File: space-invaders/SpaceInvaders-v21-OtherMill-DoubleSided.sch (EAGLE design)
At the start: 26 parts, among them J2-J4 TM4C123GXL, J3-J1 TM4C123GXL, J5 NOKIA_5110, J6 NOKIA_5110, J7 9V, U1 LM7805CT

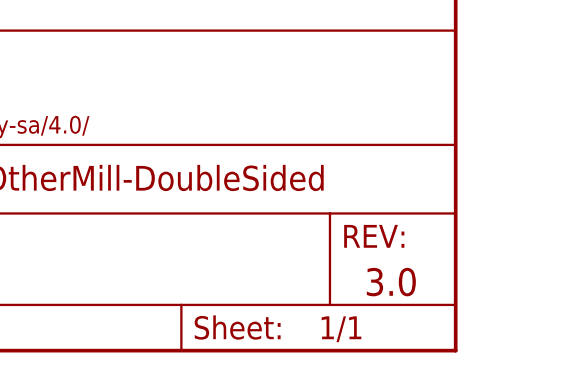
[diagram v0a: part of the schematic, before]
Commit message: Add versions to file names & Edit stuff
Add versions to file names.
Center Nokia5110 & Edit traces thereof.
Add holes for 9V battery's wires to come through.
v2.1: Replace "SpaceInvaders," "by PhiL," and the sprite icon by Top &
Bottom layers.
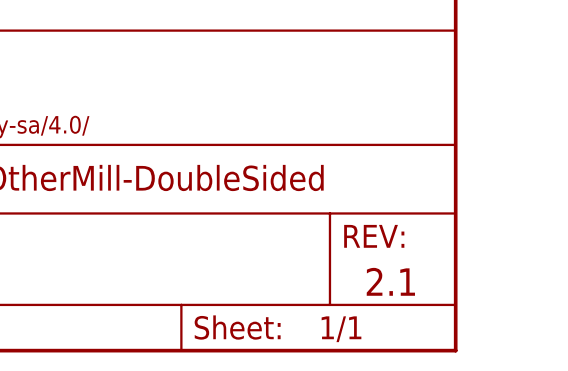
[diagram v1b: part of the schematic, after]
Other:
- note added: "2.1"
- note removed: "3.0"
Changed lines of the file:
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@@
 <plain>
 <text x="172.72" y="12.7" size="3.048" layer="94" font="vector" align="center-left">Phi Luu</text>
-<text x="238.76" y="7.62" size="3.048" layer="94" font="vector" align="center-left">3.0</text>
+<text x="238.76" y="7.62" size="3.048" layer="94" font="vector" align="center-left">2.1</text>
 <text x="134.62" y="147.32" size="1.778" layer="96" font="vector" rot="R90">PB0</text>
 <text x="132.08" y="147.32" size="1.778" layer="96" font="vector" rot="R90">PB1</text>

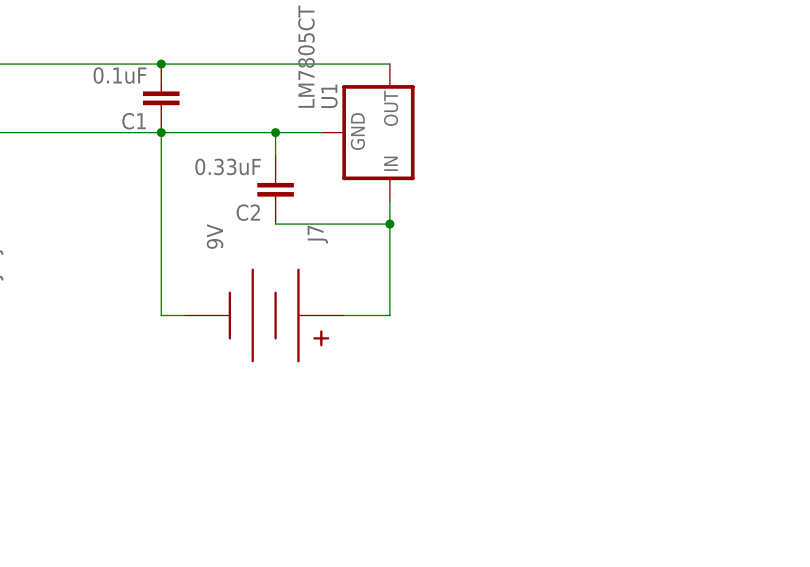
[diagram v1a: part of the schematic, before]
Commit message: Add SPDT power switch
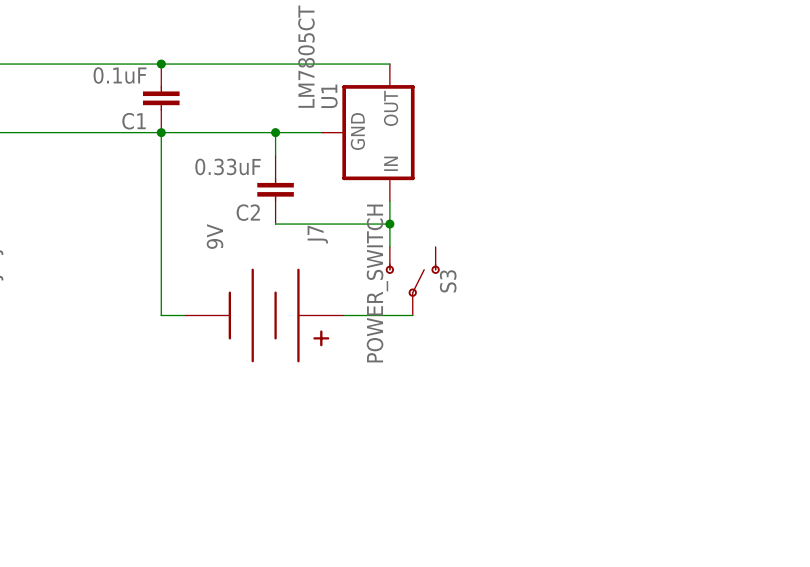
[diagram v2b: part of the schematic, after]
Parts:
- added S3: POWER_SWITCH, SparkFun-Switches:SWITCH-SPDT-PTH-11.6X4.0MM
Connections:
- new net VIN: J7.V+, S3.P
- net 9V: now also S3.S; no longer J7.V+
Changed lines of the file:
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@@
 <?xml version="1.0" encoding="utf-8"?>
 <!DOCTYPE eagle SYSTEM "eagle.dtd">
-<eagle version="8.0.1">
+<eagle version="8.0.2">
 <drawing>
 <settings>
@@
 <part name="S1" library="SparkFun-Switches" deviceset="MOMENTARY-SWITCH-SPST" device="-PTH-6.0MM" value="SPECIAL"/>
 <part name="S2" library="SparkFun-Switches" deviceset="MOMENTARY-SWITCH-SPST" device="-PTH-6.0MM" value="REGULAR"/>
+<part name="S3" library="SparkFun-Switches" deviceset="SWITCH-SPDT" device="-PTH-11.6X4.0MM" value="POWER_SWITCH"/>
 </parts>
 <sheets>
@@
 <instance part="S1" gate="G$1" x="101.6" y="50.8"/>
 <instance part="S2" gate="G$1" x="121.92" y="50.8"/>
+<instance part="S3" gate="1" x="190.5" y="101.6" rot="MR90"/>
 </instances>
 <busses>
@@
 <wire x1="187.96" y1="109.22" x2="187.96" y2="111.76" width="0.1524" layer="91"/>
 <wire x1="175.26" y1="109.22" x2="187.96" y2="109.22" width="0.1524" layer="91"/>
-<wire x1="187.96" y1="99.06" x2="187.96" y2="109.22" width="0.1524" layer="91"/>
+<pinref part="S3" gate="1" pin="S"/>
+<wire x1="187.96" y1="106.68" x2="187.96" y2="109.22" width="0.1524" layer="91"/>
 <junction x="187.96" y="109.22"/>
-<pinref part="J7" gate="G$1" pin="V+"/>
-<wire x1="182.88" y1="99.06" x2="187.96" y2="99.06" width="0.1524" layer="91"/>
 </segment>
 </net>
@@
 </segment>
 </net>
+<net name="VIN" class="1">
+<segment>
+<pinref part="J7" gate="G$1" pin="V+"/>
+<wire x1="182.88" y1="99.06" x2="190.5" y2="99.06" width="0.1524" layer="91"/>
+<pinref part="S3" gate="1" pin="P"/>
+</segment>
+</net>

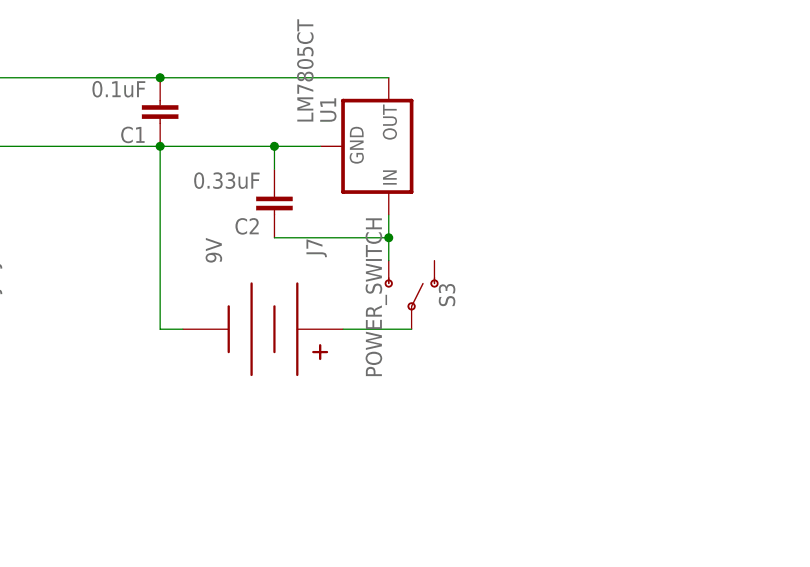
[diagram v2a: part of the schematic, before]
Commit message: Change pin position SPDT slide switch
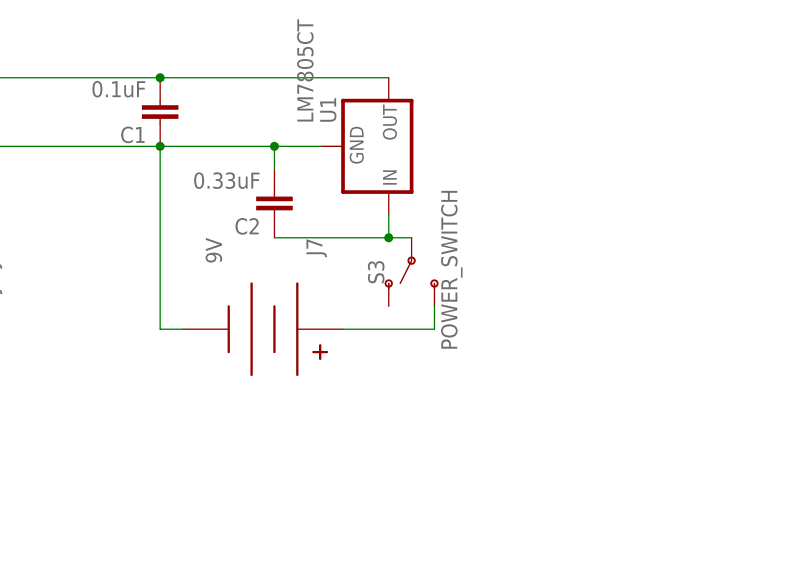
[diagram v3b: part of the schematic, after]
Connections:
- net 9V: now also J7.V+; no longer C2.1, U1.IN
- net VIN: now also C2.1, U1.IN; no longer J7.V+
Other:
- moved on the sheet: S3
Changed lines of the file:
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@@
 <instance part="S1" gate="G$1" x="101.6" y="50.8"/>
 <instance part="S2" gate="G$1" x="121.92" y="50.8"/>
-<instance part="S3" gate="1" x="190.5" y="101.6" rot="MR90"/>
+<instance part="S3" gate="1" x="190.5" y="106.68" rot="MR270"/>
 </instances>
 <busses>
@@
 </segment>
 </net>
-<net name="9V" class="1">
+<net name="VIN" class="1">
 <segment>
 <pinref part="U1" gate="G$1" pin="IN"/>
@@
 <wire x1="187.96" y1="109.22" x2="187.96" y2="111.76" width="0.1524" layer="91"/>
 <wire x1="175.26" y1="109.22" x2="187.96" y2="109.22" width="0.1524" layer="91"/>
-<pinref part="S3" gate="1" pin="S"/>
-<wire x1="187.96" y1="106.68" x2="187.96" y2="109.22" width="0.1524" layer="91"/>
+<pinref part="S3" gate="1" pin="P"/>
+<wire x1="190.5" y1="109.22" x2="187.96" y2="109.22" width="0.1524" layer="91"/>
 <junction x="187.96" y="109.22"/>
 </segment>
@@
 </segment>
 </net>
-<net name="VIN" class="1">
+<net name="9V" class="1">
 <segment>
 <pinref part="J7" gate="G$1" pin="V+"/>
-<wire x1="182.88" y1="99.06" x2="190.5" y2="99.06" width="0.1524" layer="91"/>
-<pinref part="S3" gate="1" pin="P"/>
-</segment>
-</net>
+<pinref part="S3" gate="1" pin="S"/>
+<wire x1="182.88" y1="99.06" x2="193.04" y2="99.06" width="0.1524" layer="91"/>
+<wire x1="193.04" y1="99.06" x2="193.04" y2="101.6" width="0.1524" layer="91"/>
+</segment>
+</net>
